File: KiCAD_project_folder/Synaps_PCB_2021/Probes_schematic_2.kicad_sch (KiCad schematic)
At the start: 28 parts, among them U10 LTC2452ITS8-TRMPBF, U7 LTC2452ITS8-TRMPBF, U8 LTC2452ITS8-TRMPBF, U9 LTC2452ITS8-TRMPBF

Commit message: Added library for one piece
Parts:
- renumbered C11 to C36, C12 to C37, C13 to C38, C14 to C39, C15 to C40, C16 to C41, C17 to C42, C18 to C43, C19 to C44, C20 to C45, C21 to C46, C22 to C47, C23 to C48, C24 to C49, C25 to C50, C26 to C51, C27 to C52, C28 to C53, C29 to C54, C30 to C55, C31 to C56, C32 to C57, C33 to C58, C34 to C59, U8 to U?, U9 to U?, U10 to U?, U7 to U?

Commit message: Added LTC2452 librairy
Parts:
- removed U? (x4): LTC2452ITS8-TRMPBF, TSOT-23_TS8_LIT, symbol 2021-11-05_00-54-21:LTC2452ITS8-TRMPBF
- added U10, U7, U8, U9: LTC2452ITS8-TRMPBF, TSOT-23_TS8_LIT, symbol LTC2452:LTC2452ITS8-TRMPBF
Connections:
- net +3V3: now also U10.3 (REF), U10.4 (VCC), U7.3 (REF), U7.4 (VCC), U8.3 (REF), U8.4 (VCC), U9.3 (REF), U9.4 (VCC)
- net GNDREF: now also U10.2 (GND), U10.8 (SDO), U7.2 (GND), U7.8 (SDO), U8.2 (GND), U8.8 (SDO), U9.2 (GND), U9.8 (SDO)
- net Probe5_SDO: now also U10.7 (*CS), U7.7 (*CS), U8.7 (*CS), U9.7 (*CS)
- net Probe5_~{CS}: now also U10.6 (IN+), U7.6 (IN+), U8.6 (IN+), U9.6 (IN+)
- net Probe_SCK: now also U10.1 (SCK), U7.1 (SCK), U8.1 (SCK), U9.1 (SCK)
- net sense_+: now also U10.5 (IN-), U7.5 (IN-), U8.5 (IN-), U9.5 (IN-)
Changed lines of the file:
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@@
     (pin "1")
   )
-  (symbol (lib_id "2021-11-05_00-54-21:LTC2452ITS8-TRMPBF") (at 182.88 39.37 0) (unit 1)
-    (in_bom yes) (on_board yes)
-    (property "Reference" "U?" (id 0) (at 210.82 29.5402 0)
+  (symbol (lib_id "LTC2452:LTC2452ITS8-TRMPBF") (at 182.88 134.62 0) (unit 1)
+    (in_bom yes) (on_board yes) (fields_autoplaced)
+    (property "Reference" "U10" (id 0) (at 210.82 125.3924 0)
       (effects (font (size 1.524 1.524)))
     )
-    (property "Value" "LTC2452ITS8-TRMPBF" (id 1) (at 210.82 32.2326 0)
+    (property "Value" "LTC2452ITS8-TRMPBF" (id 1) (at 210.82 128.3858 0)
+      (effects (font (size 1.524 1.524)))
+    )
+    (property "Footprint" "TSOT-23_TS8_LIT" (id 2) (at 210.82 128.524 0)
+      (effects (font (size 1.524 1.524)) hide)
+    )
+    (property "Datasheet" "" (id 3) (at 182.88 134.62 0)
+      (effects (font (size 1.524 1.524)))
+    )
+    (pin "1")
+    (pin "2")
+    (pin "3")
+    (pin "4")
+    (pin "5")
+    (pin "6")
+    (pin "7")
+    (pin "8")
+  )
+  (symbol (lib_id "LTC2452:LTC2452ITS8-TRMPBF") (at 53.34 162.56 0) (unit 1)
+    (in_bom yes) (on_board yes) (fields_autoplaced)
+    (property "Reference" "U7" (id 0) (at 81.28 153.3324 0)
+      (effects (font (size 1.524 1.524)))
+    )
+    (property "Value" "LTC2452ITS8-TRMPBF" (id 1) (at 81.28 156.3258 0)
+      (effects (font (size 1.524 1.524)))
+    )
+    (property "Footprint" "TSOT-23_TS8_LIT" (id 2) (at 81.28 156.464 0)
+      (effects (font (size 1.524 1.524)) hide)
+    )
+    (property "Datasheet" "" (id 3) (at 53.34 162.56 0)
+      (effects (font (size 1.524 1.524)))
+    )
+    (pin "1")
+    (pin "2")
+    (pin "3")
+    (pin "4")
+    (pin "5")
+    (pin "6")
+    (pin "7")
+    (pin "8")
+  )
+  (symbol (lib_id "LTC2452:LTC2452ITS8-TRMPBF") (at 182.88 39.37 0) (unit 1)
+    (in_bom yes) (on_board yes) (fields_autoplaced)
+    (property "Reference" "U8" (id 0) (at 210.82 30.1424 0)
+      (effects (font (size 1.524 1.524)))
+    )
+    (property "Value" "LTC2452ITS8-TRMPBF" (id 1) (at 210.82 33.1358 0)
       (effects (font (size 1.524 1.524)))
     )
@@
       (effects (font (size 1.524 1.524)))
     )
+    (pin "1")
+    (pin "2")
+    (pin "3")
+    (pin "4")
+    (pin "5")
+    (pin "6")
+    (pin "7")
+    (pin "8")
   )
-  (symbol (lib_id "2021-11-05_00-54-21:LTC2452ITS8-TRMPBF") (at 182.88 88.9 0) (unit 1)
-    (in_bom yes) (on_board yes)
-    (property "Reference" "U?" (id 0) (at 210.82 79.0702 0)
+  (symbol (lib_id "LTC2452:LTC2452ITS8-TRMPBF") (at 182.88 88.9 0) (unit 1)
+    (in_bom yes) (on_board yes) (fields_autoplaced)
+    (property "Reference" "U9" (id 0) (at 210.82 79.6724 0)
       (effects (font (size 1.524 1.524)))
     )
-    (property "Value" "LTC2452ITS8-TRMPBF" (id 1) (at 210.82 81.7626 0)
+    (property "Value" "LTC2452ITS8-TRMPBF" (id 1) (at 210.82 82.6658 0)
       (effects (font (size 1.524 1.524)))
     )
@@
       (effects (font (size 1.524 1.524)))
     )
-  )
-  (symbol (lib_id "2021-11-05_00-54-21:LTC2452ITS8-TRMPBF") (at 182.88 134.62 0) (unit 1)
-    (in_bom yes) (on_board yes)
-    (property "Reference" "U?" (id 0) (at 210.82 124.7902 0)
-      (effects (font (size 1.524 1.524)))
-    )
-    (property "Value" "LTC2452ITS8-TRMPBF" (id 1) (at 210.82 127.4826 0)
-      (effects (font (size 1.524 1.524)))
-    )
-    (property "Footprint" "TSOT-23_TS8_LIT" (id 2) (at 210.82 128.524 0)
-      (effects (font (size 1.524 1.524)) hide)
-    )
-    (property "Datasheet" "" (id 3) (at 182.88 134.62 0)
-      (effects (font (size 1.524 1.524)))
-    )
-  )
-  (symbol (lib_id "2021-11-05_00-54-21:LTC2452ITS8-TRMPBF") (at 53.34 162.56 0) (unit 1)
-    (in_bom yes) (on_board yes)
-    (property "Reference" "U?" (id 0) (at 81.28 152.7302 0)
-      (effects (font (size 1.524 1.524)))
-    )
-    (property "Value" "LTC2452ITS8-TRMPBF" (id 1) (at 81.28 155.4226 0)
-      (effects (font (size 1.524 1.524)))
-    )
-    (property "Footprint" "TSOT-23_TS8_LIT" (id 2) (at 81.28 156.464 0)
-      (effects (font (size 1.524 1.524)) hide)
-    )
-    (property "Datasheet" "" (id 3) (at 53.34 162.56 0)
-      (effects (font (size 1.524 1.524)))
-    )
+    (pin "1")
+    (pin "2")
+    (pin "3")
+    (pin "4")
+    (pin "5")
+    (pin "6")
+    (pin "7")
+    (pin "8")
   )
 )

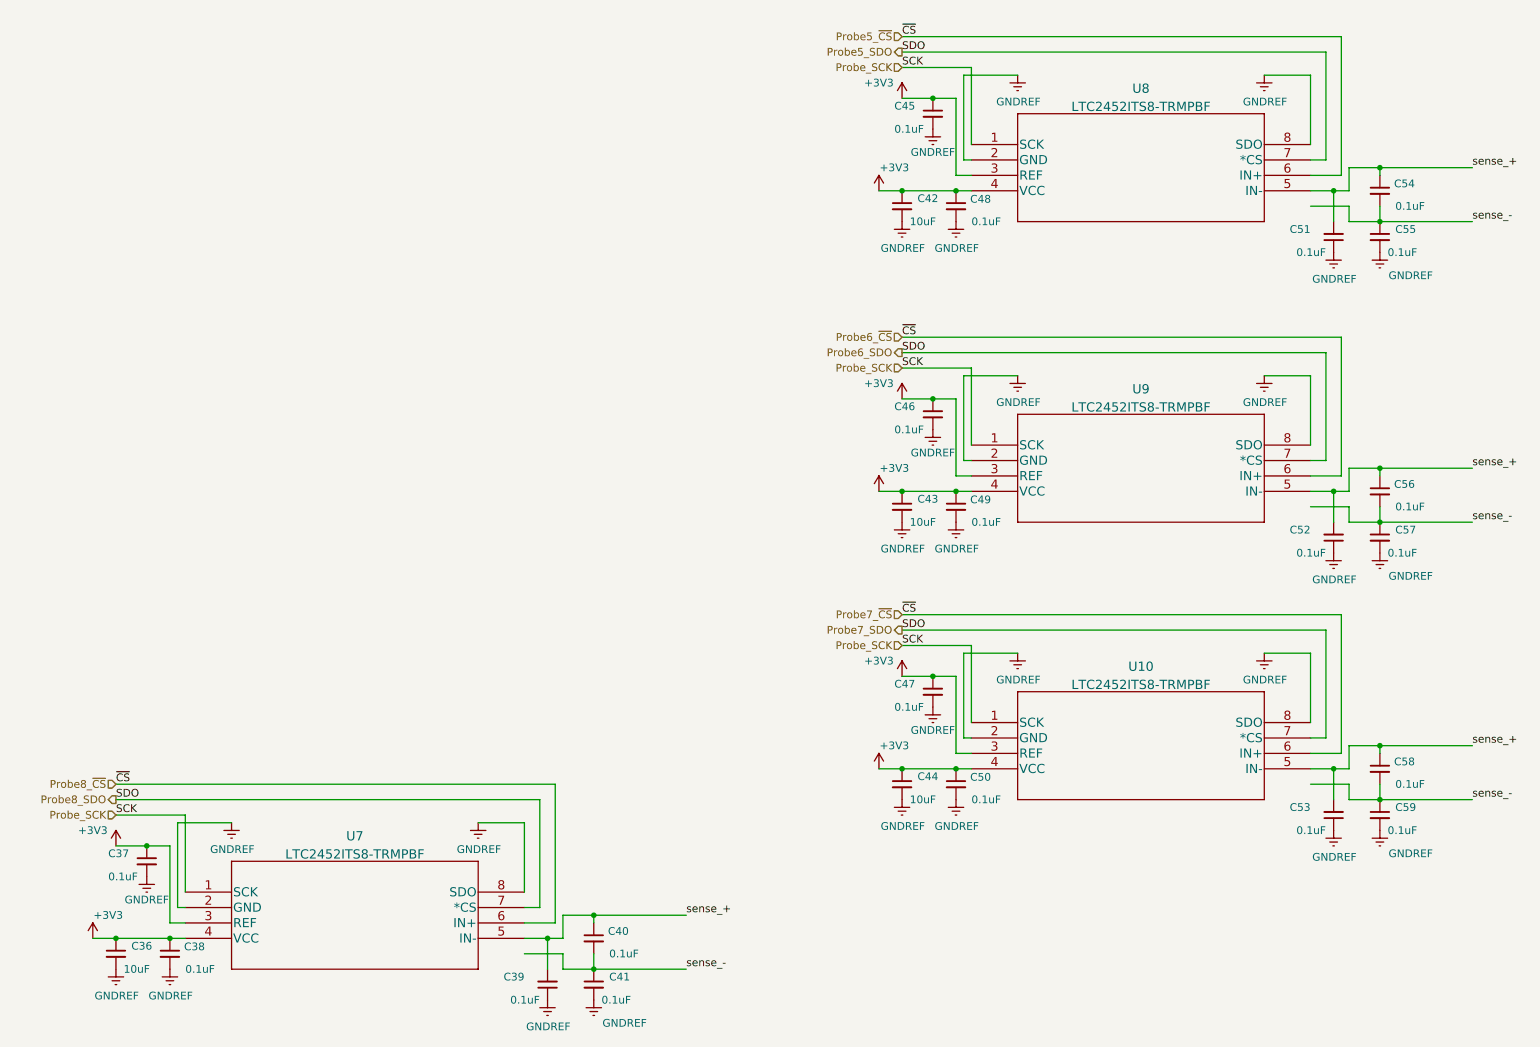
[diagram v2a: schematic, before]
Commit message: Added basic PCB guidelines
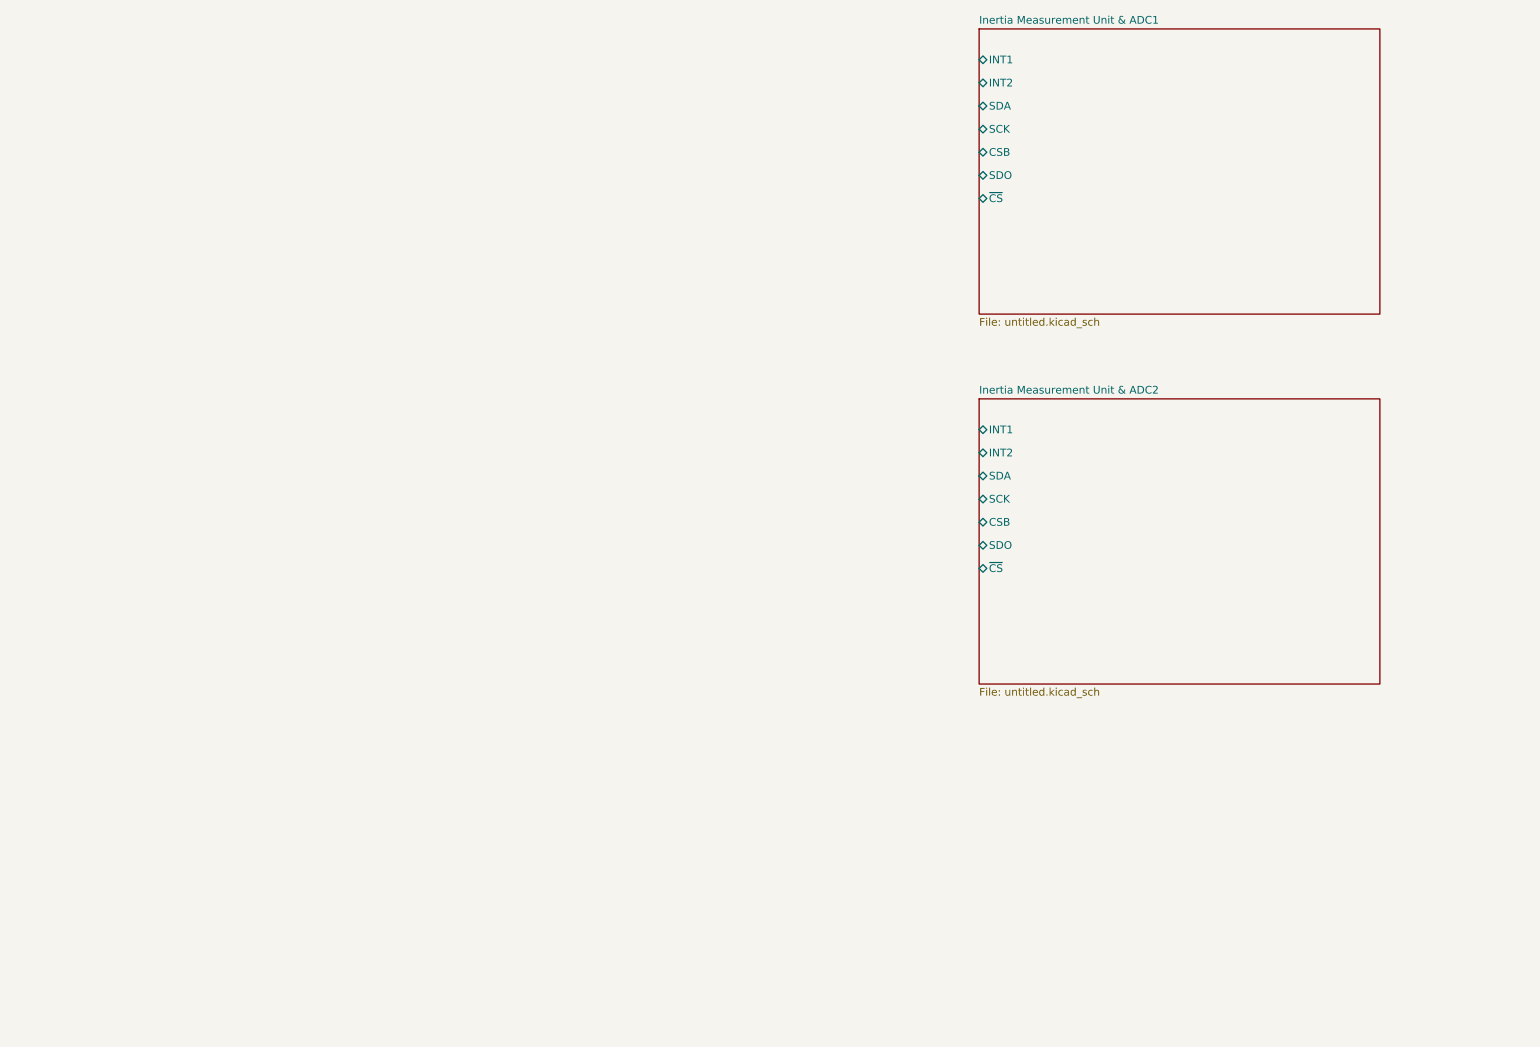
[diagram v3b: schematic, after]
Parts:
- removed C36, C42, C43, C44: 10uF, symbol Device:C_Small
- removed C37, C38, C39, C40, C41, C45, C46, C47, C48, C49, C50, C51, C52, C53, C54, C55, C56, C57, C58, C59: 0.1uF, symbol Device:C_Small
- removed U10, U7, U8, U9: LTC2452ITS8-TRMPBF, TSOT-23_TS8_LIT, symbol LTC2452:LTC2452ITS8-TRMPBF
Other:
- added sheet Inertia Measurement Unit & ADC1 (untitled.kicad_sch)
- added sheet Inertia Measurement Unit & ADC2 (untitled.kicad_sch)
